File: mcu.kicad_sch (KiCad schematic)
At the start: 15 parts, among them U1 STM32U535CETx, U3 AT25SF081-SSHD-X

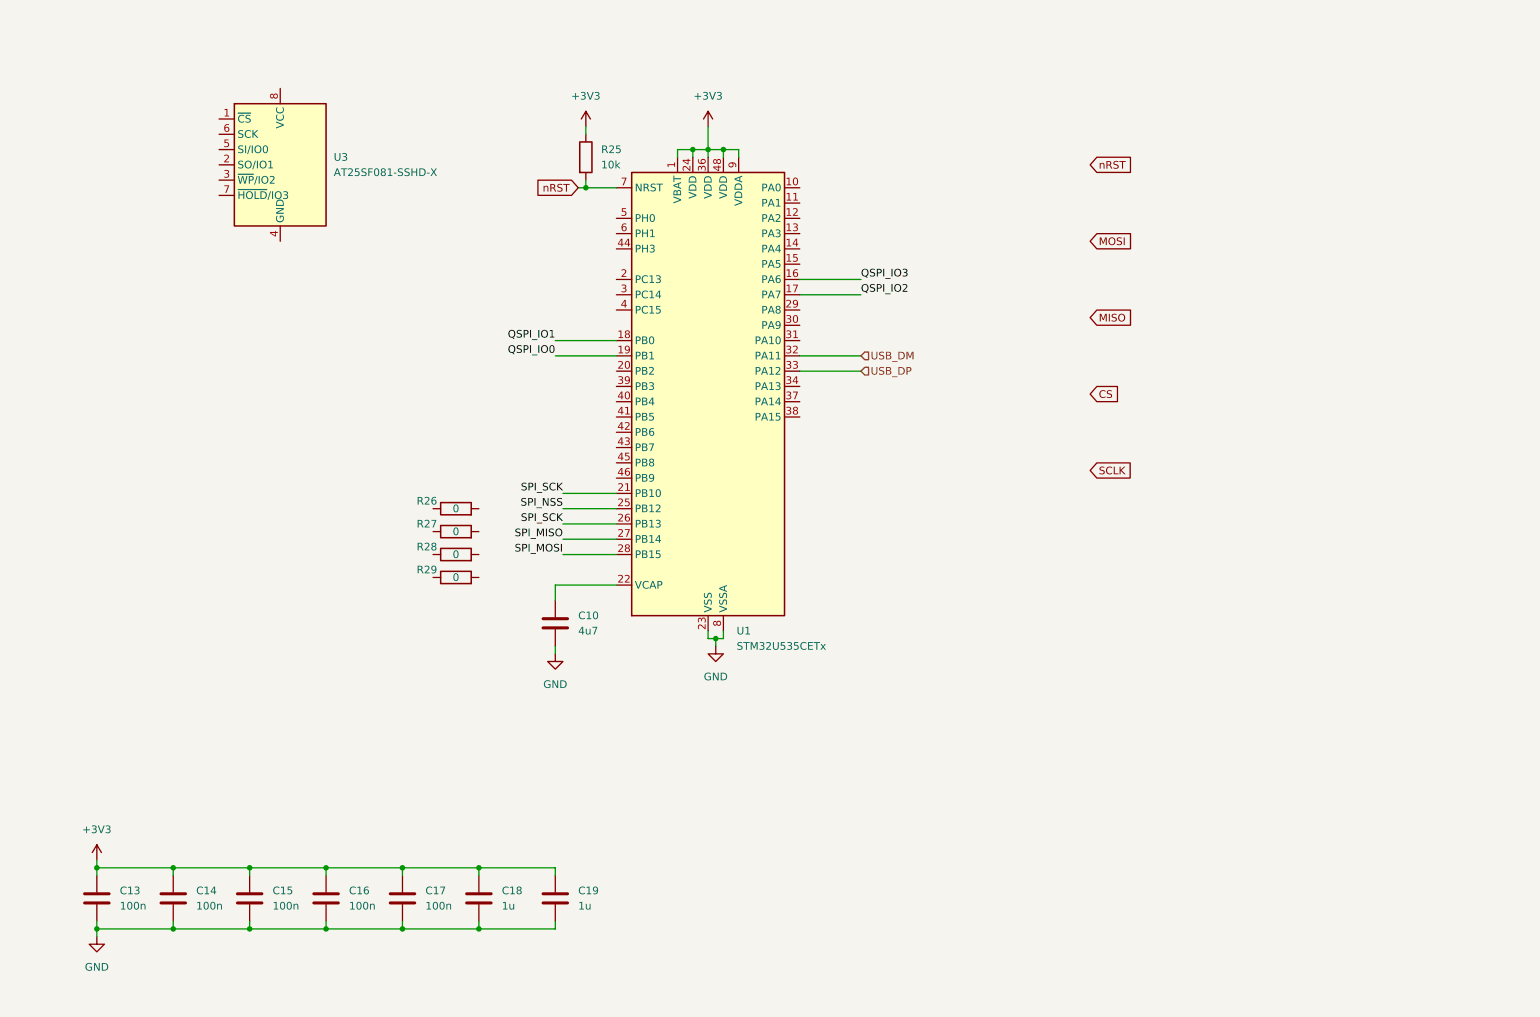
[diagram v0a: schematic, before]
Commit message: Initial MCU IO pinout defined. USB and power sheet created
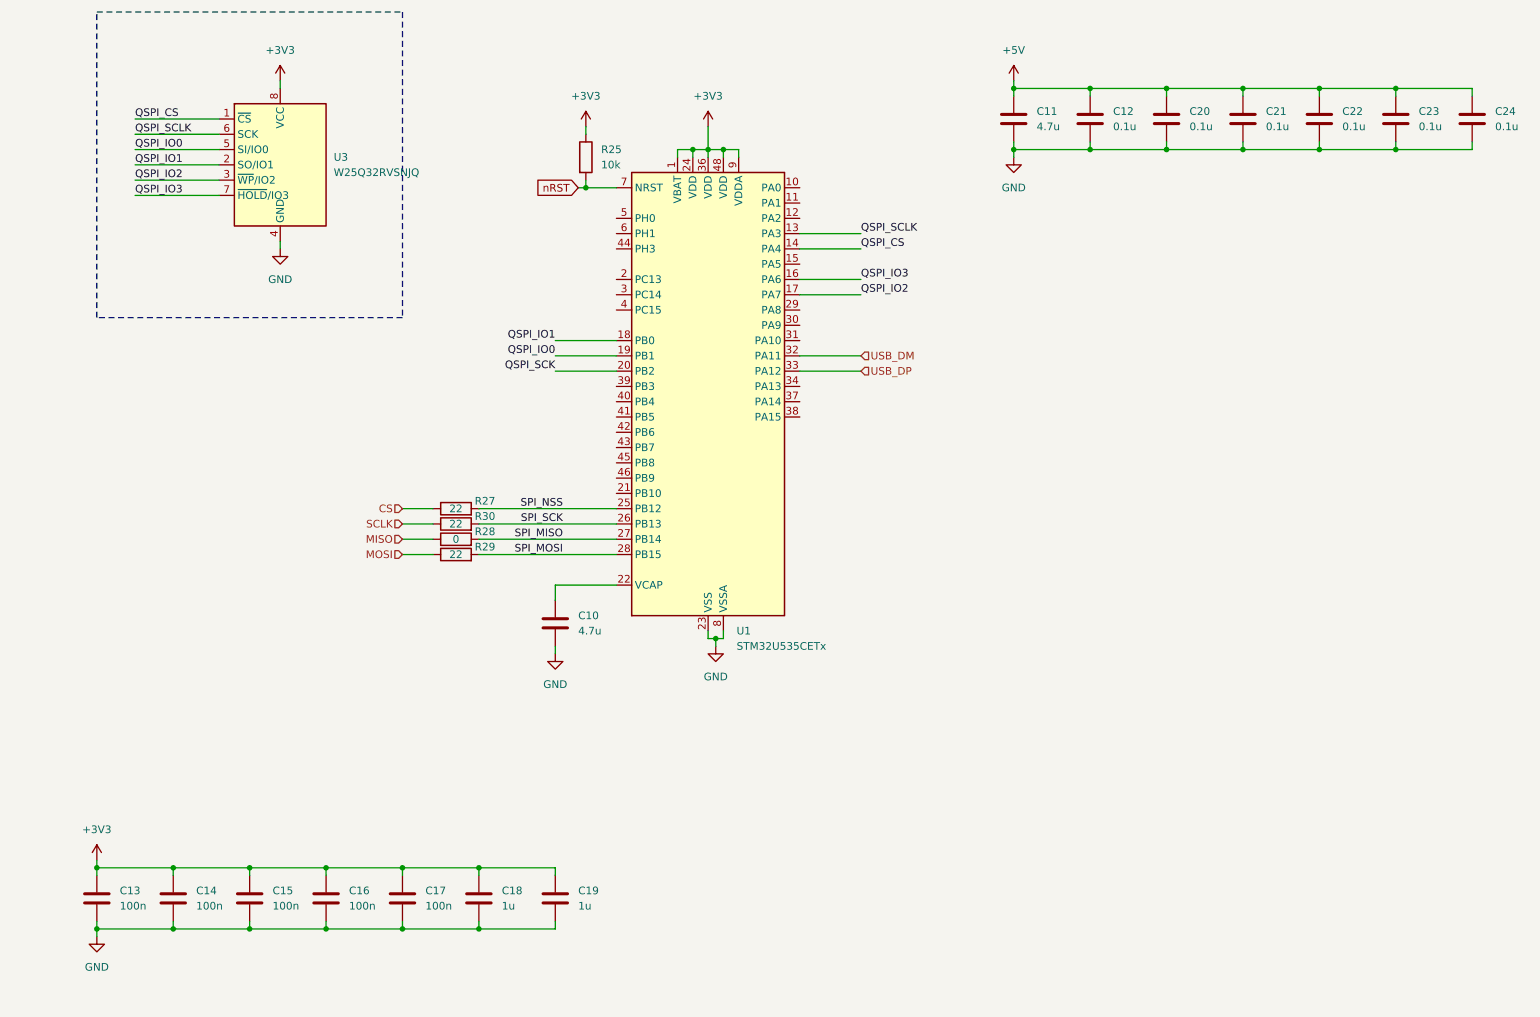
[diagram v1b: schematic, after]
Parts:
- removed R26: 0, symbol Device:R
- added C11: 4.7u, symbol Device:C
- added C12, C20, C21, C22, C23, C24: 0.1u, symbol Device:C
- added R30: 22, symbol Device:R
- C10: value 4u7 -> 4.7u
- R27, R29: value 0 -> 22
- U3: value AT25SF081-SSHD-X -> W25Q32RVSNJQ
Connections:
- net +3V3: now also U3.8 (VCC)
- net CS: now also R27.1
- net GND: now also U3.4 (GND), C11.2, C12.2, C20.2, C21.2, C22.2, C23.2, C24.2
- net MISO: now also R28.1
- net MOSI: now also R29.1
- net QSPI_IO0: now also U3.5 (SI/IO0)
- net QSPI_IO1: now also U3.2 (SO/IO1)
- net QSPI_IO2: now also U3.3 (~{WP}/IO2)
- net QSPI_IO3: now also U3.7 (~{HOLD}/IO3)
- net SCLK: now also R30.1
- net SPI_MISO: now also R28.2
- net SPI_MOSI: now also R29.2
- net SPI_NSS: now also R27.2
- net SPI_SCK: now also R30.2; no longer U1.21 (PB10)
- net QSPI_SCLK: now reaches U1.13 (PA3)
- net QSPI_SCLK: now also U3.6 (SCK)
- net QSPI_CS: now reaches U1.14 (PA4)
- net QSPI_CS: now also U3.1 (~{CS})
- net QSPI_SCK: now reaches U1.20 (PB2)
- new net +5V: C11.1, C12.1, C20.1, C21.1, C22.1, C23.1, C24.1
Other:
- moved on the sheet: R27, R29

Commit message: sch_0v1 ready for review
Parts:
- removed C11: 4.7u, symbol Device:C
- removed C12, C20, C21, C22, C23, C24: 0.1u, symbol Device:C
- removed R25: 10k, symbol Device:R
- removed R28: 0, symbol Device:R
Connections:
- net SPI_MISO is gone; now on net MISO: U1.27 (PB14)
- net PB4: now reaches U1.40 (PB4)
- net PB5: now reaches U1.41 (PB5)
- net PB6: now reaches U1.42 (PB6)
- net PB7: now reaches U1.43 (PB7)
- net PB8: now reaches U1.45 (PB8)
- net QSPI_SCK: no longer names the net of U1.20 (PB2)
- net SPI_MOSI: no longer names the net of R29.2, U1.28 (PB15)
- net SPI_NSS: no longer names the net of R27.2, U1.25 (PB12)
- net SPI_SCK: no longer names the net of R30.2, U1.26 (PB13)
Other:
- note added: "Decoupling - MCU, QSPI"
- note added: "MCU"
- note added: "QSPI"
- moved on the sheet: C10, C13, C14, C15, C16, C17, C18, C19, R27, R29, R30, U1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
